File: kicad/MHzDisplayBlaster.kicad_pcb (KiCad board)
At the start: 2 copper layers, 50 x 39 mm, 9 parts, among them J1 Conn_02x15 DigitLHS, J2 Conn_02x15 DigitRHS, J3 Conn_01x03_Pin, J4 Conn_01x02_Pin, U1 DC56-11GWA, U2 74LS04

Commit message: Switch to 74HC04
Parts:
- U2: value 74LS04 -> 74HC04
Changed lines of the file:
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@@
+    )
+  )
+  (footprint "Resistor_THT:R_Axial_DIN0204_L3.6mm_D1.6mm_P5.08mm_Horizontal" (layer "B.Cu")
+    (at 148.04 60.5 180)
+    (descr "Resistor, Axial_DIN0204 series, Axial, Horizontal, pin pitch=5.08mm, 0.167W, length*diameter=3.6*1.6mm^2, http://cdn-reichelt.de/documents/datenblatt/B400/1_4W%23YAG.pdf")
+    (tags "Resistor Axial_DIN0204 series Axial Horizontal pin pitch 5.08mm 0.167W length 3.6mm diameter 1.6mm")
+    (property "Sheetfile" "MHzDisplayBlaster.kicad_sch")
+    (property "Sheetname" "")
+    (property "ki_description" "Resistor")
+    (property "ki_keywords" "R res resistor")
+    (attr through_hole)
+    (fp_text reference "R3" (at 2.54 1.75) (layer "B.SilkS")
+        (effects (font (size 1 1) (thickness 0.15)) (justify mirror))
+    )
+    (fp_text value "330" (at 2.54 -1.92) (layer "B.Fab")
+        (effects (font (size 1 1) (thickness 0.15)) (justify mirror))
+    )
+    (fp_text user "${REFERENCE}" (at 2.54 0) (layer "B.Fab")
+        (effects (font (size 0.72 0.72) (thickness 0.108)) (justify mirror))
+    )
+    (fp_line (start 0.62 -0.92) (end 4.46 -0.92)
+      (stroke (width 0.12) (type solid)) (layer "B.SilkS"))
+    (fp_line (start 0.62 0.92) (end 4.46 0.92)
+      (stroke (width 0.12) (type solid)) (layer "B.SilkS"))
+    (fp_line (start -0.95 -1.05) (end 6.03 -1.05)
+      (stroke (width 0.05) (type solid)) (layer "B.CrtYd"))
+    (fp_line (start -0.95 1.05) (end -0.95 -1.05)
+      (stroke (width 0.05) (type solid)) (layer "B.CrtYd"))
+    (fp_line (start 6.03 -1.05) (end 6.03 1.05)
+      (stroke (width 0.05) (type solid)) (layer "B.CrtYd"))
+    (fp_line (start 6.03 1.05) (end -0.95 1.05)
+      (stroke (width 0.05) (type solid)) (layer "B.CrtYd"))
+    (fp_line (start 0 0) (end 0.74 0)
+      (stroke (width 0.1) (type solid)) (layer "B.Fab"))
+    (fp_line (start 0.74 -0.8) (end 4.34 -0.8)
+      (stroke (width 0.1) (type solid)) (layer "B.Fab"))
+    (fp_line (start 0.74 0.8) (end 0.74 -0.8)
+      (stroke (width 0.1) (type solid)) (layer "B.Fab"))
+    (fp_line (start 4.34 -0.8) (end 4.34 0.8)
+      (stroke (width 0.1) (type solid)) (layer "B.Fab"))
+    (fp_line (start 4.34 0.8) (end 0.74 0.8)
+      (stroke (width 0.1) (type solid)) (layer "B.Fab"))
+    (fp_line (start 5.08 0) (end 4.34 0)
+      (stroke (width 0.1) (type solid)) (layer "B.Fab"))
+    (pad "1" thru_hole circle (at 0 0 180) (size 1.4 1.4) (drill 0.7) (layers "*.Cu" "*.Mask")
+      (net 22 "Net-(J4-Pin_2)") (pintype "passive"))
+    (pad "2" thru_hole oval (at 5.08 0 180) (size 1.4 1.4) (drill 0.7) (layers "*.Cu" "*.Mask")
+      (net 3 "2") (pintype "passive"))
+    (model "${KICAD6_3DMODEL_DIR}/Resistor_THT.3dshapes/R_Axial_DIN0204_L3.6mm_D1.6mm_P5.08mm_Horizontal.wrl"
+      (offset (xyz 0 0 0))
+      (scale (xyz 1 1 1))
+      (rotate (xyz 0 0 0))
     )
   )
@@
     (property "Sheetname" "")
     (property "ki_description" "Hex Inverter")
-    (property "ki_keywords" "TTL not inv")
+    (property "ki_keywords" "HCMOS not inv")
     (attr smd)
-    (fp_text reference "U2" (at 0.025 -5.31) (layer "B.SilkS")
+    (fp_text reference "U2" (at 0 -5.173249) (layer "B.SilkS")
         (effects (font (size 1 1) (thickness 0.15)) (justify mirror))
     )
-    (fp_text value "74LS04" (at 0 -5.28) (layer "B.Fab")
+    (fp_text value "74HC04" (at 0 -5.28) (layer "B.Fab")
         (effects (font (size 1 1) (thickness 0.15)) (justify mirror))
     )
@@
       (offset (xyz 0 0 0))
       (scale (xyz 1 1 1))
-      (rotate (xyz 0 0 0))
-    )
-  )
-  (footprint "Resistor_THT:R_Axial_DIN0204_L3.6mm_D1.6mm_P5.08mm_Horizontal" (layer "B.Cu")
-    (at 148.04 60.5 180)
-    (descr "Resistor, Axial_DIN0204 series, Axial, Horizontal, pin pitch=5.08mm, 0.167W, length*diameter=3.6*1.6mm^2, http://cdn-reichelt.de/documents/datenblatt/B400/1_4W%23YAG.pdf")
-    (tags "Resistor Axial_DIN0204 series Axial Horizontal pin pitch 5.08mm 0.167W length 3.6mm diameter 1.6mm")
-    (property "Sheetfile" "MHzDisplayBlaster.kicad_sch")
-    (property "Sheetname" "")
-    (property "ki_description" "Resistor")
-    (property "ki_keywords" "R res resistor")
-    (attr through_hole)
-    (fp_text reference "R3" (at 2.54 1.75) (layer "B.SilkS")
-        (effects (font (size 1 1) (thickness 0.15)) (justify mirror))
-    )
-    (fp_text value "330" (at 2.54 -1.92) (layer "B.Fab")
-        (effects (font (size 1 1) (thickness 0.15)) (justify mirror))
-    )
-    (fp_text user "${REFERENCE}" (at 2.54 0) (layer "B.Fab")
-        (effects (font (size 0.72 0.72) (thickness 0.108)) (justify mirror))
-    )
-    (fp_line (start 0.62 -0.92) (end 4.46 -0.92)
-      (stroke (width 0.12) (type solid)) (layer "B.SilkS"))
-    (fp_line (start 0.62 0.92) (end 4.46 0.92)
-      (stroke (width 0.12) (type solid)) (layer "B.SilkS"))
-    (fp_line (start -0.95 -1.05) (end 6.03 -1.05)
-      (stroke (width 0.05) (type solid)) (layer "B.CrtYd"))
-    (fp_line (start -0.95 1.05) (end -0.95 -1.05)
-      (stroke (width 0.05) (type solid)) (layer "B.CrtYd"))
-    (fp_line (start 6.03 -1.05) (end 6.03 1.05)
-      (stroke (width 0.05) (type solid)) (layer "B.CrtYd"))
-    (fp_line (start 6.03 1.05) (end -0.95 1.05)
-      (stroke (width 0.05) (type solid)) (layer "B.CrtYd"))
-    (fp_line (start 0 0) (end 0.74 0)
-      (stroke (width 0.1) (type solid)) (layer "B.Fab"))
-    (fp_line (start 0.74 -0.8) (end 4.34 -0.8)
-      (stroke (width 0.1) (type solid)) (layer "B.Fab"))
-    (fp_line (start 0.74 0.8) (end 0.74 -0.8)
-      (stroke (width 0.1) (type solid)) (layer "B.Fab"))
-    (fp_line (start 4.34 -0.8) (end 4.34 0.8)
-      (stroke (width 0.1) (type solid)) (layer "B.Fab"))
-    (fp_line (start 4.34 0.8) (end 0.74 0.8)
-      (stroke (width 0.1) (type solid)) (layer "B.Fab"))
-    (fp_line (start 5.08 0) (end 4.34 0)
-      (stroke (width 0.1) (type solid)) (layer "B.Fab"))
-    (pad "1" thru_hole circle (at 0 0 180) (size 1.4 1.4) (drill 0.7) (layers "*.Cu" "*.Mask")
-      (net 22 "Net-(J4-Pin_2)") (pintype "passive"))
-    (pad "2" thru_hole oval (at 5.08 0 180) (size 1.4 1.4) (drill 0.7) (layers "*.Cu" "*.Mask")
-      (net 3 "2") (pintype "passive"))
-    (model "${KICAD6_3DMODEL_DIR}/Resistor_THT.3dshapes/R_Axial_DIN0204_L3.6mm_D1.6mm_P5.08mm_Horizontal.wrl"
-      (offset (xyz 0 0 0))
-      (scale (xyz 1 1 1))

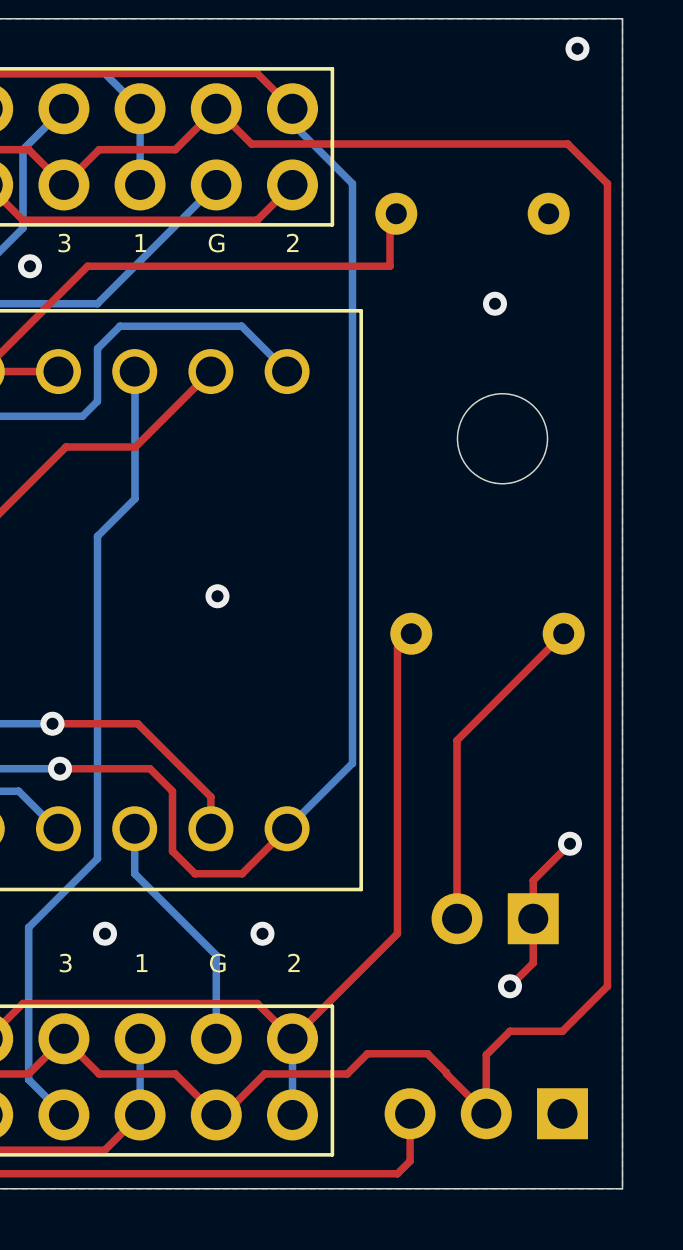
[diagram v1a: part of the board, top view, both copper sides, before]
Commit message: Added 2N7000 MOSFET for LED header. KiCad 8
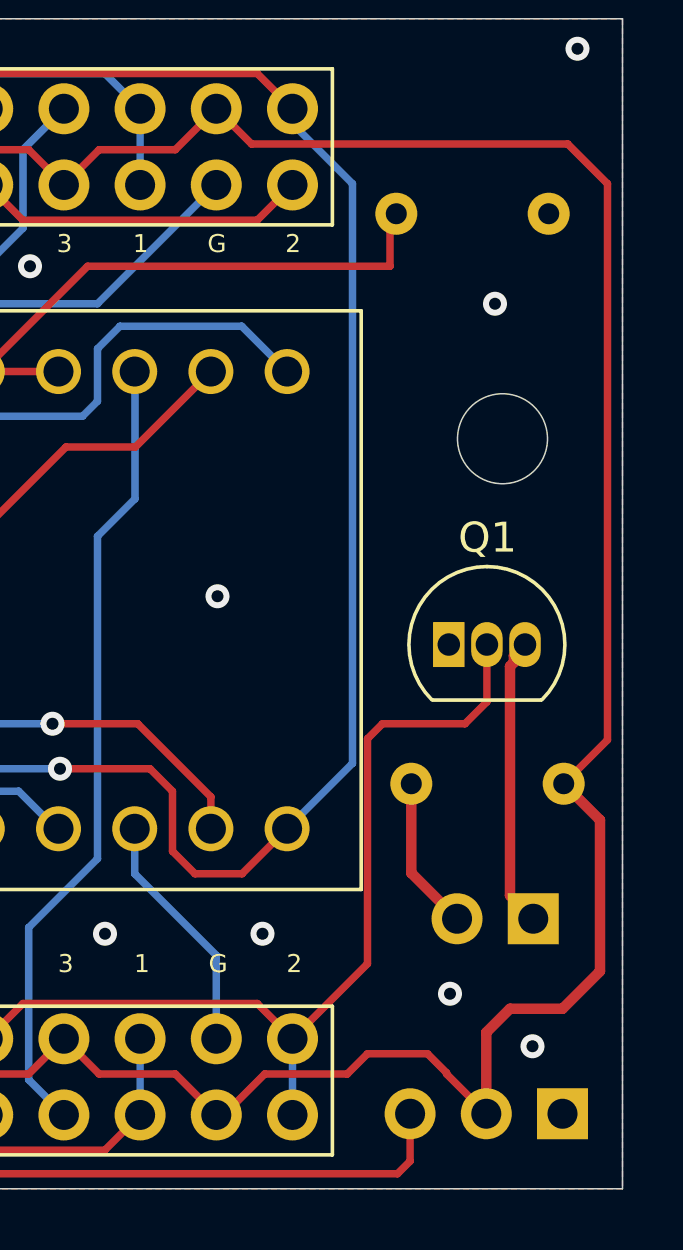
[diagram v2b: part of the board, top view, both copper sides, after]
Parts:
- added Q1: 2N7000, Package_TO_SOT_THT:TO-92_Inline, F.Cu at (144.2, 60.9)
- moved R3 7.13 mm to (143.0, 65.5), turned to 0 degrees
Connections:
- J4 pad 1: GND -> Net-(J4-Pin_1)
- R3 pad 2: 2 -> 3
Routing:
- net Net-(J4-Pin_1): track 0.00 -> 9.67 mm
- net Net-(J4-Pin_2): track 11.0 -> 5.13 mm
- net GND: track 5.58 -> 0.00 mm
- net 2: track 150.5 -> 152.8 mm
- net 3: track 151.1 -> 152.1 mm
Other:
- board text added: "-LED+"
- board text removed: "LED+"
- board text removed: "LED-"
